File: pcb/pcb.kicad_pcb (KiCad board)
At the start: 2 copper layers, 90 x 99.5 mm, 24 parts

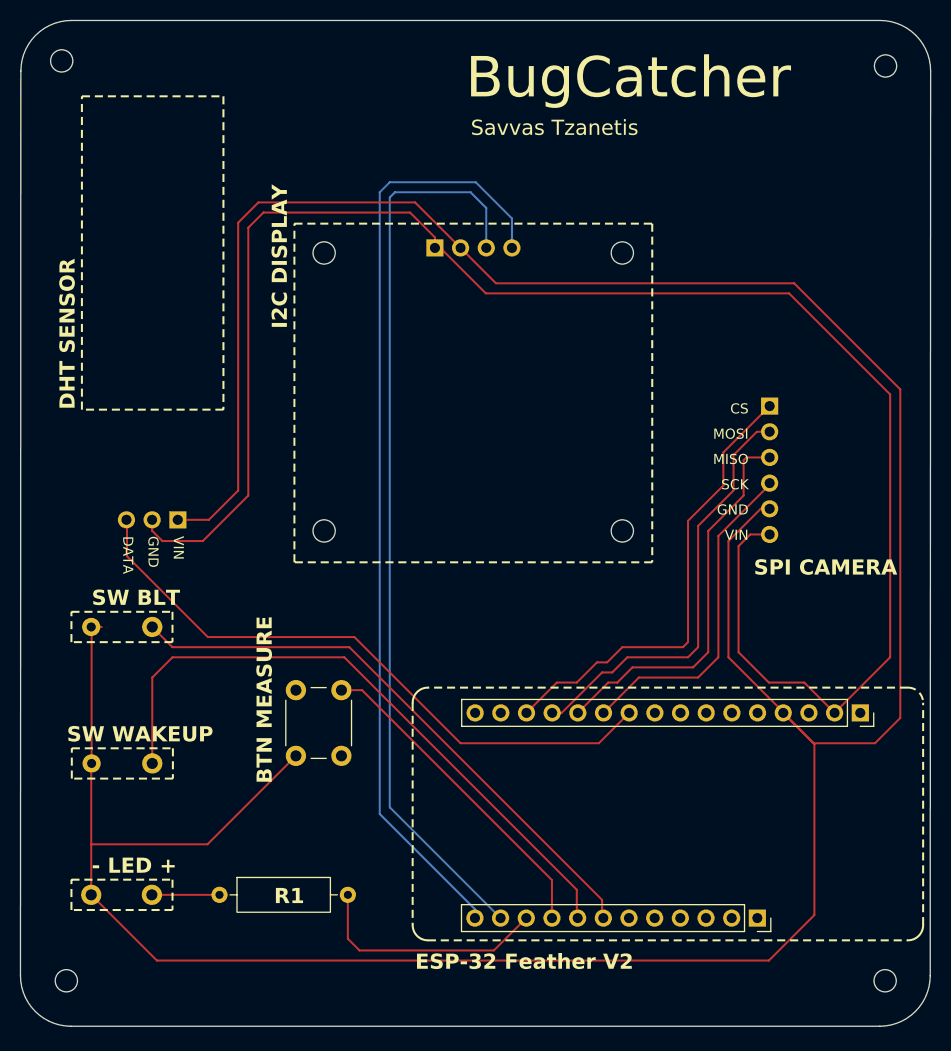
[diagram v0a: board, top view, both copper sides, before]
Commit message: Integrated Arducam library with the rest of the code, updated PCB and schematic
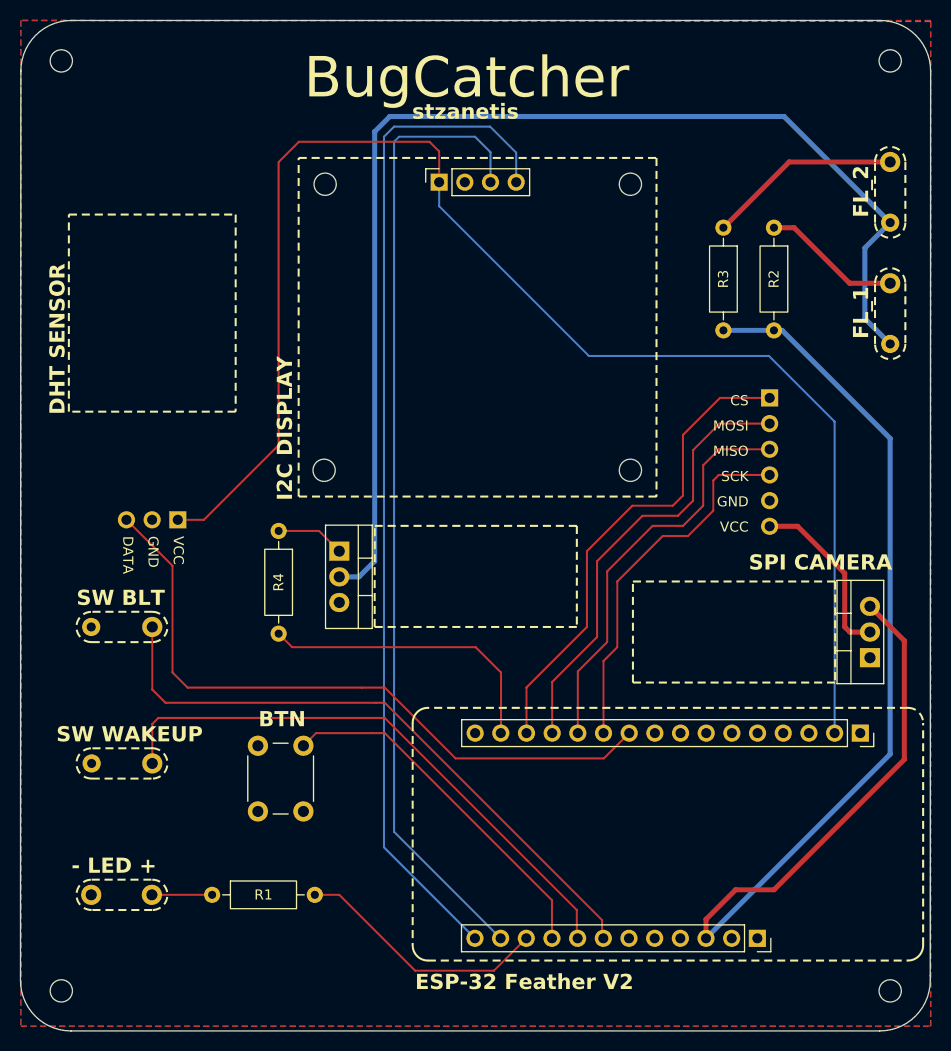
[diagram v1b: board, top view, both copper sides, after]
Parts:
- removed the ? at (157.6, 67.0)
- removed the ? at (155.0, 67.0)
- removed the ? at (152.5, 67.0)
- removed the ? at (150.0, 67.0)
- removed the REF** at (128.7, 131.0)
- added ?: , , F.Cu at (195.0, 58.5)
- added ?: , , F.Cu at (195.0, 76.5)
- added ?: , , F.Cu at (195.0, 70.5)
- added ?: , , F.Cu at (195.0, 64.5)
- added Q2: TIP120, Package_TO_SOT_THT:TO-220-3_Vertical, F.Cu at (140.5, 97.0)
- added REF**: R_Axial_DIN0207_L6.3mm_D2.5mm_P10.16mm_Horizontal, Resistor_THT:R_Axial_DIN0207_L6.3mm_D2.5mm_P10.16mm_Horizontal, F.Cu at (183.5, 65.0)
- added REF**: R_Axial_DIN0207_L6.3mm_D2.5mm_P10.16mm_Horizontal, Resistor_THT:R_Axial_DIN0207_L6.3mm_D2.5mm_P10.16mm_Horizontal, F.Cu at (134.5, 95.0)
- added REF**: R_Axial_DIN0207_L6.3mm_D2.5mm_P10.16mm_Horizontal, Resistor_THT:R_Axial_DIN0207_L6.3mm_D2.5mm_P10.16mm_Horizontal, F.Cu at (127.9, 131.0)
- added REF**: PinSocket_1x04_P2.54mm_Vertical, Connector_PinSocket_2.54mm:PinSocket_1x04_P2.54mm_Vertical, F.Cu at (150.4, 60.5)
- added REF**: LD1117, Package_TO_SOT_THT:TO-220-3_Vertical, F.Cu at (193.0, 107.5)
- added REF**: R_Axial_DIN0207_L6.3mm_D2.5mm_P10.16mm_Horizontal, Resistor_THT:R_Axial_DIN0207_L6.3mm_D2.5mm_P10.16mm_Horizontal, F.Cu at (178.5, 65.0)
- moved REF** 6.85 mm to (169.3, 60.7)
- moved REF** 6.80 mm to (139.1, 60.7)
- moved REF** 6.66 mm to (136.9, 116.2)
- moved REF** 6.05 mm to (169.3, 89.0)
- moved REF** 6.00 mm to (139.0, 89.0)
- moved REF** 2.00 mm to (181.9, 135.3)
- moved REF** 2.00 mm to (192.0, 115.0)
- moved REF** 1.12 mm to (195.0, 140.5)
- moved REF** 1.12 mm to (113.0, 140.5)
- moved REF** 0.81 mm to (183.1, 81.8)
- moved REF** 0.68 mm to (195.0, 48.5)
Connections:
- ? pad 2: (no net) -> GND (x3)
- ? pad 1: (no net) -> LED_0
- ? pad 1: (no net) -> SW_BLT
- ? pad 1: (no net) -> SW_WAKEUP
- REF** pad 10: (no net) -> LED
- REF** pad 11: (no net) -> SCL
- REF** pad 12: (no net) -> SDA
- REF** pad 3: (no net) -> VIN
- REF** pad 7: (no net) -> SW_BLT
- REF** pad 8: (no net) -> SW_WAKEUP
- REF** pad 9: (no net) -> BTN_MEASURE
- REF** pad 1: (no net) -> CS
- REF** pad 2: (no net) -> MOSI
- REF** pad 3: (no net) -> MISO
- REF** pad 4: (no net) -> SCK
- REF** pad 5: (no net) -> GND
- REF** pad 6: (no net) -> CAMERA_VCC
- REF** pad 1: (no net) -> BTN_MEASURE
- REF** pad 2: (no net) -> GND (x2)
- REF** pad 1: (no net) -> VCC
- REF** pad 3: (no net) -> DATA
- REF** pad 10: (no net) -> DATA
- REF** pad 11: (no net) -> SCK
- REF** pad 12: (no net) -> MISO
- REF** pad 13: (no net) -> MOSI
- REF** pad 14: (no net) -> CS
- REF** pad 15: (no net) -> GATE
- REF** pad 2: (no net) -> VCC
- REF** pad 4: (no net) -> GND
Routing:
- net (no net): track 1088.2 -> 0.00 mm
- net VCC: track 0.00 -> 142.6 mm
- net VIN: track 0.00 -> 122.5 mm
- net DRAIN: track 0.00 -> 116.8 mm
- net SDA: track 0.00 -> 101.0 mm
- net SCL: track 0.00 -> 97.1 mm
- net DATA: track 0.00 -> 66.7 mm
- net SW_BLT: track 0.00 -> 62.0 mm
- net SW_WAKEUP: track 0.00 -> 56.9 mm
- net CS: track 0.00 -> 48.3 mm
- net MOSI: track 0.00 -> 44.5 mm
- net MISO: track 0.00 -> 40.6 mm
- net SCK: track 0.00 -> 36.8 mm
- net BTN_MEASURE: track 0.00 -> 35.7 mm
- net GATE: track 0.00 -> 29.6 mm
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- added copper zone on B.Cu, net GND
- added copper zone on F.Cu, net GND
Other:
- board size 90 x 99.5 mm -> 90 x 100 mm
- board text added: "BTN"
- board text added: "FL_1"
- board text added: "FL_2"
- board text added: "VCC"
- board text added: "stzanetis"
- board text removed: "BTN MEASURE"
- board text removed: "R1"
- board text removed: "Savvas Tzanetis"
- board text removed: "VIN"
